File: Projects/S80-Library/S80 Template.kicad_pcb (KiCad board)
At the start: 2 copper layers, 1 part

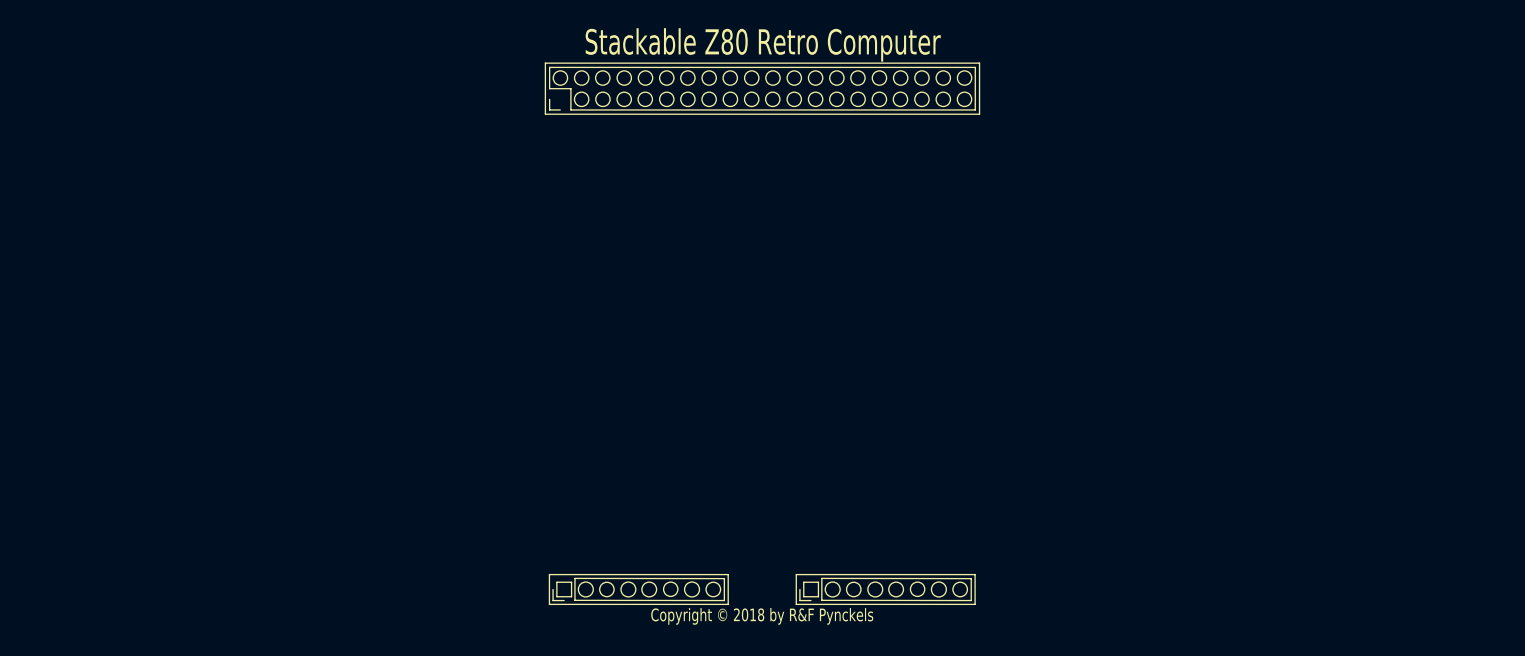
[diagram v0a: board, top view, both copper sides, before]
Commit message: added the template
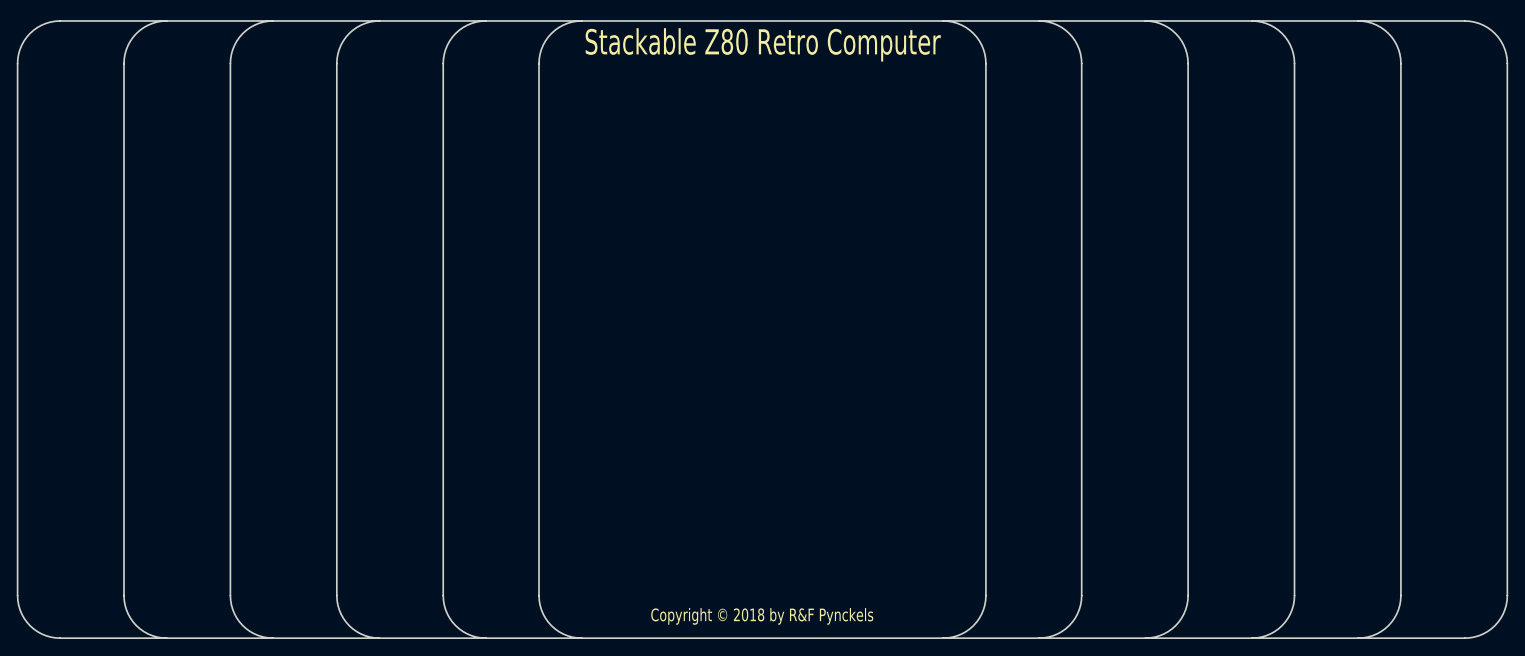
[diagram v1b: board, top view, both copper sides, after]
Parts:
- removed G***: LOGO, Pynckels:pi
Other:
- board outline added: 177.8 x 73.7 mm
- board text removed: "This PCB is fabricated by JLCPCB (batch n° JLCJLCJLCJLC)"
